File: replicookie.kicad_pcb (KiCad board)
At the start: 4 copper layers, 160 x 120 mm, 161 parts, among them J1001 Conn_01x08_Female, J1002 Screw_Terminal_01x04, J1003 Conn_02x03_Odd_Even, J1004 Conn_01x08_Female, J1101 Conn_01x08_Female, J1102 Screw_Terminal_01x04, J1103 Conn_02x03_Odd_Even, J1104 Conn_01x08_Female, J1201 Conn_01x08_Female, J1202 Screw_Terminal_01x04, J1203 Conn_02x03_Odd_Even, J1204 Conn_01x08_Female, J1301 Conn_01x08_Female, J1302 Screw_Terminal_01x04, J1303 Conn_02x03_Odd_Even, J1304 Conn_01x08_Female, J1401 Conn_01x08_Female, J1402 Screw_Terminal_01x04, J1403 Conn_02x03_Odd_Even, J1404 Conn_01x08_Female, J1501 Conn_01x08_Female, J1502 Screw_Terminal_01x04, J1503 Conn_02x03_Odd_Even, J1504 Conn_01x08_Female, J2 TFM-115-01-F-D-A, J3 TFM-120-01-F-D-A, J301 USB_B_Micro, J401 JK0654219, J501 USB_A, J502 USB_A, J801 Conn_01x08_Female, J802 Screw_Terminal_01x04, J803 Conn_02x03_Odd_Even, J804 Conn_01x08_Female, J901 Conn_01x08_Female, J902 Screw_Terminal_01x04, J903 Conn_02x03_Odd_Even, J904 Conn_01x08_Female, U201 DS1307ZN+, U301 93LCxxBxxOT, U302 FT4232H, U401 MIC33050-4YHL, U402 KSZ9031RNXCA, U403 ASDMB-25.000MHz, U404 74LVC2G07, U501 ASDMB-24.000MHz-C, U502 ASDMB-26.000MHz-C, U503 USB3343, U504 74LVC1G07, U505 USB2514B_Bi, U601 TCA9800, X201 ASE-xxxMHz, Y301 ABM8-12.000MHZ-20

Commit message: Expand PCB, change to inches, center Snickerdoodle
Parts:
- removed R308: 4.7k, Resistor_SMD:R_0603_1608Metric
- removed R309: 10k, Resistor_SMD:R_0603_1608Metric
- added H101: MountingHole, MountingHole:MountingHole_3mm, F.Cu at (130.2, 200.0)
- added H102: MountingHole, MountingHole:MountingHole_3mm, F.Cu at (308.0, 200.0)
- added H103: MountingHole, MountingHole:MountingHole_3mm, F.Cu at (130.2, 79.4)
- added H104: MountingHole, MountingHole:MountingHole_3mm, F.Cu at (308.0, 79.4)
- R301, R302, R303, R304, R305, R306, R307: footprint Resistor_SMD:R_0603_1608Metric -> Resistor_SMD:R_0402_1005Metric
- moved C314 133.5 mm to (144.3, 111.8), turned to -90 degrees
- moved C304 133.5 mm to (142.7, 111.8), turned to -90 degrees
- moved C306 131.6 mm to (133.9, 107.2), turned to 180 degrees
- moved R305 124.6 mm to (136.4, 89.9), turned to 180 degrees
- moved C313 122.2 mm to (144.3, 95.0), turned to 90 degrees
- moved Y301 112.0 mm to (138.2, 113.0), turned to 90 degrees
- moved R306 108.3 mm to (145.3, 111.8), turned to 90 degrees
- moved R307 107.8 mm to (151.4, 101.9)
- moved J301 82.1 mm to (129.7, 91.2), turned to -90 degrees
- moved C401 29.7 mm to (291.0, 132.5)
- moved C402 29.7 mm to (284.2, 132.2)
- moved C403 29.7 mm to (284.2, 135.0)
- moved C404 29.7 mm to (277.7, 135.0)
- moved C405 29.7 mm to (276.0, 135.0)
- moved C406 29.7 mm to (269.2, 123.0)
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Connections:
- net /FTDI/DM renamed /FTDI/D-
- net /FTDI/DP renamed /FTDI/D+
- net Net-(C304-Pad1) renamed /FTDI/VPLL
- net Net-(C305-Pad1) renamed /FTDI/VPHY
- net Net-(R305-Pad1) renamed /FTDI/REF
- net Net-(R306-Pad2) renamed /FTDI/~FTDI_RESET
- U302 pad 26: Net-(U302-Pad26) -> /SWCLK
- U302 pad 27: Net-(U302-Pad27) -> Net-(R307-Pad1)
- U302 pad 28: Net-(U302-Pad28) -> /SWDIO
- U302 pad 29: Net-(U302-Pad29) -> /MCU_~RST
- U302 pad 38: /SWCLK -> /FTDI/FTDI_TX
- U302 pad 39: Net-(R307-Pad1) -> /FTDI/FTDI_RX
- U302 pad 40: /SWDIO -> Net-(U302-Pad40)
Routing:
- net /Ethernet/TXRXB+: track 42.8 -> 0.00 mm
- net /Ethernet/TXRXA-: track 38.9 -> 0.00 mm
- net /Ethernet/TXRXA+: track 38.6 -> 0.00 mm
- net /Ethernet/TXRXB-: track 38.3 -> 0.00 mm
- net /Ethernet/TXRXD+: track 37.0 -> 0.00 mm
- net /Ethernet/TXRXC+: track 35.7 -> 0.00 mm
- net /Ethernet/TXRXD-: track 42.3 -> 7.62 mm
- net /Ethernet/TXRXC-: track 37.2 -> 4.97 mm
- net +3V3: track 30.9 -> 4.85 mm, vias 11 -> 4
- net /Ethernet/LED1: track 21.4 -> 0.00 mm
- net /ETHERNET.MDIO: track 20.1 -> 0.00 mm, vias 1 -> 0
- net /Ethernet/DVDDL: track 23.4 -> 3.31 mm, vias 11 -> 0
- net /ETHERNET.TXD0: track 17.6 -> 0.00 mm
- net /ETHERNET.MDC: track 17.1 -> 0.00 mm, vias 1 -> 0
- net /ETHERNET.TXD1: track 16.1 -> 0.00 mm
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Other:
- board size 160 x 120 mm -> 184.1 x 127 mm

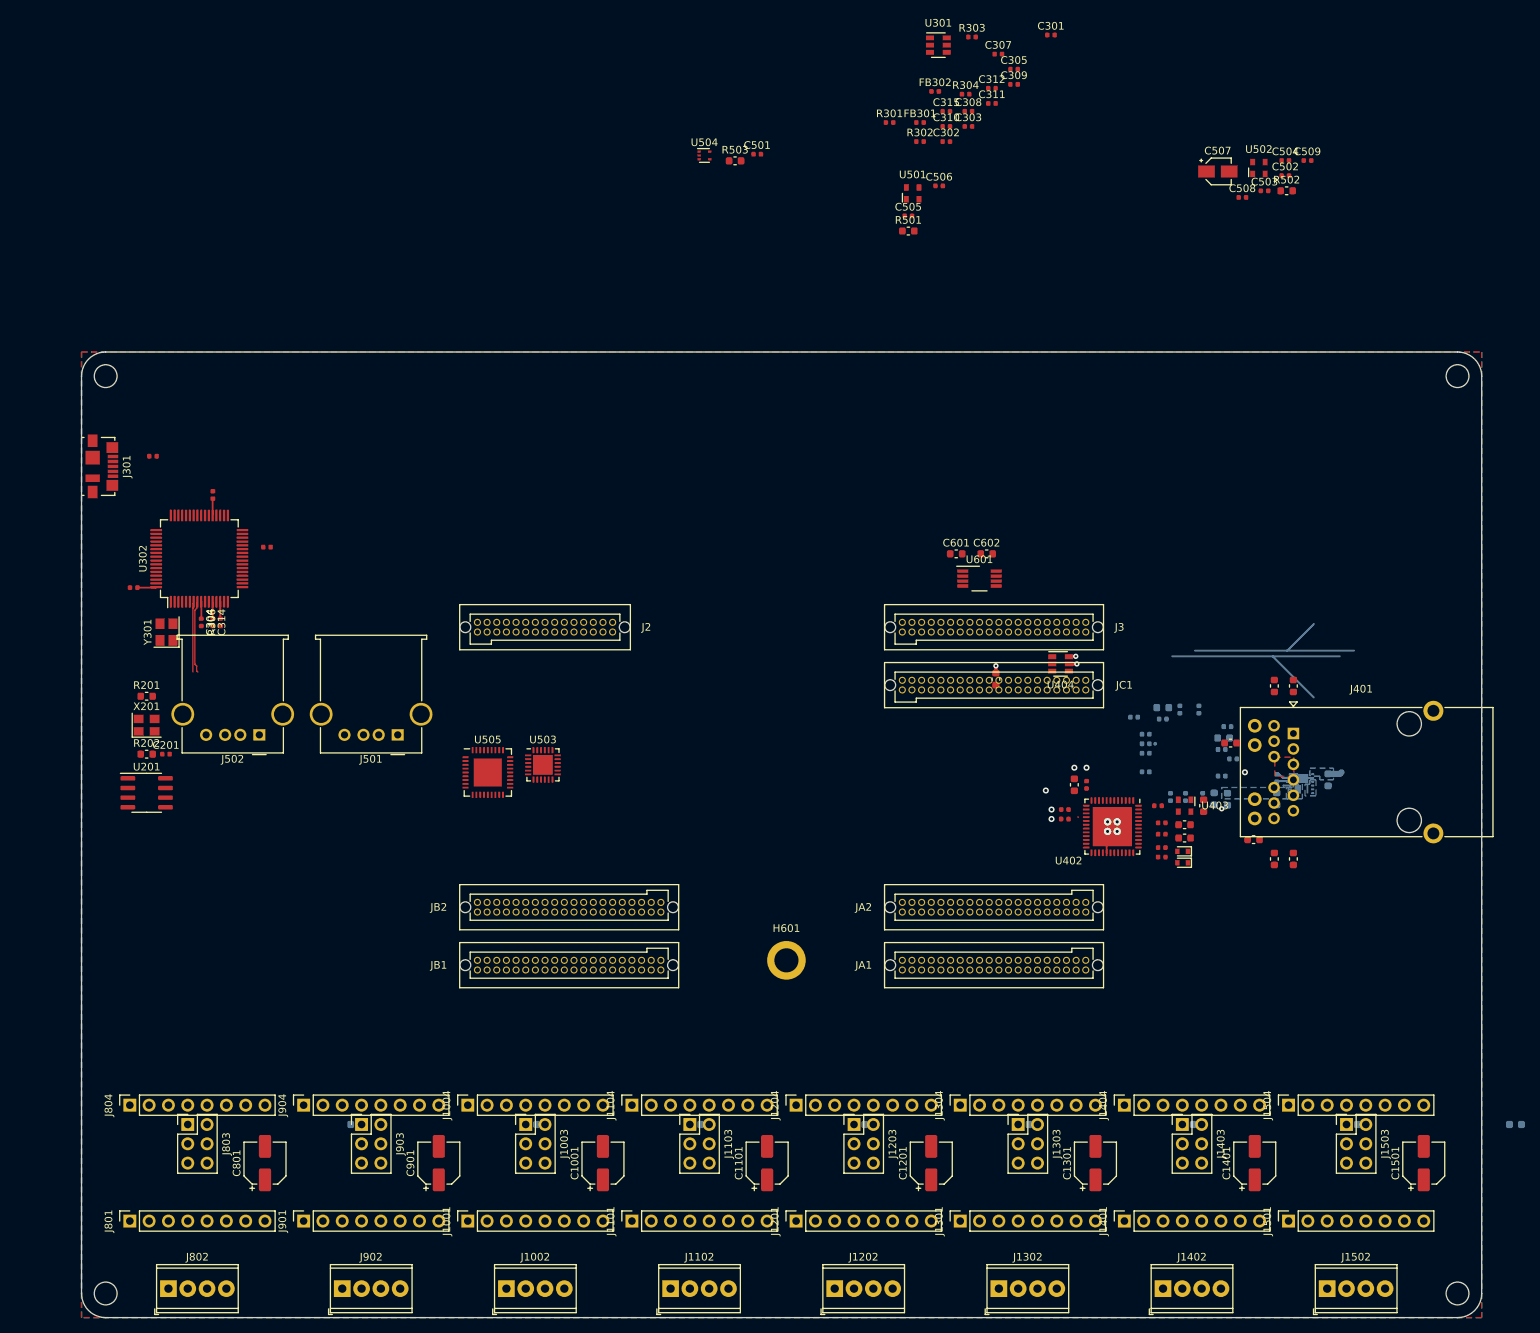
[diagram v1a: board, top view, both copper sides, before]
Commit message: Move Ethernet PHY to left side of board
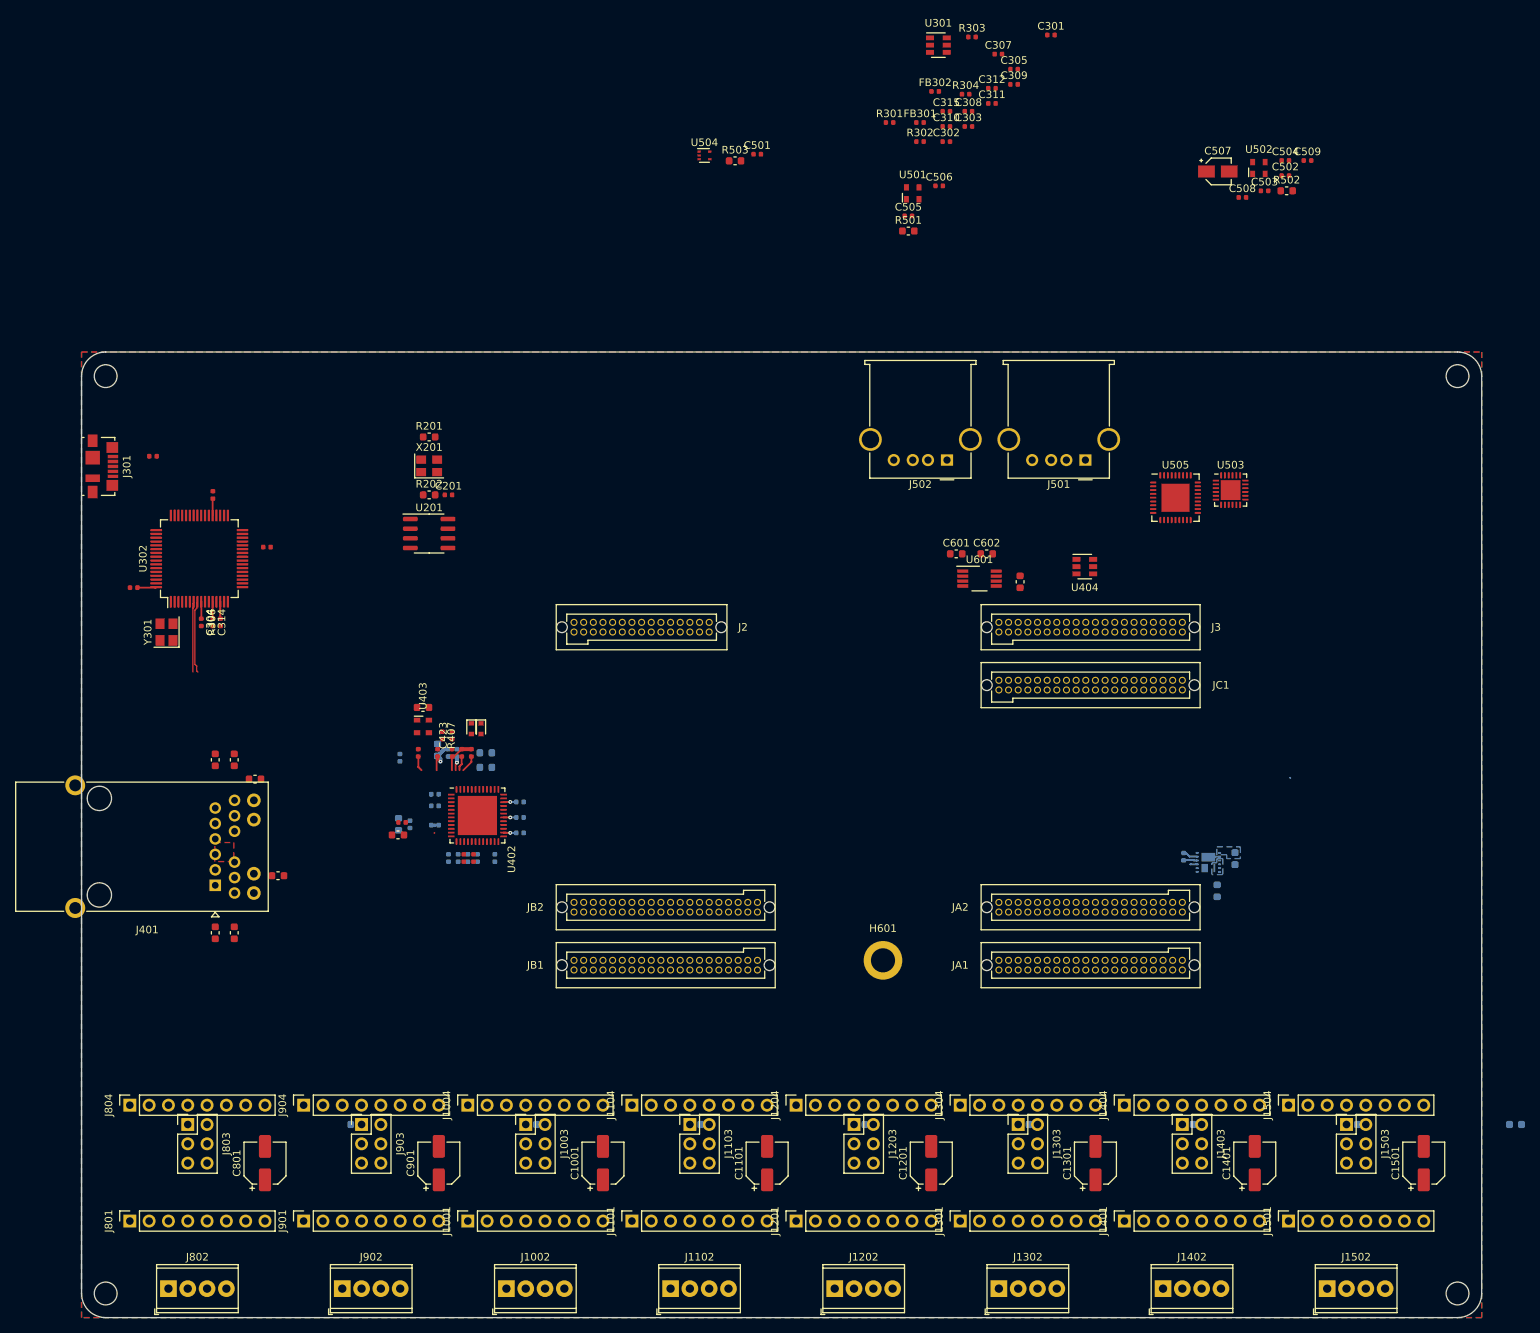
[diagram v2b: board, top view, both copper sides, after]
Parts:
- C423: footprint Capacitor_SMD:C_0603_1608Metric -> Capacitor_SMD:C_0402_1005Metric
- R407: footprint Resistor_SMD:R_0603_1608Metric -> Resistor_SMD:R_0402_1005Metric
- moved C426 145.5 mm to (144.6, 152.6), turned to -90 degrees
- moved J401 143.2 mm to (144.6, 146.3), turned to 180 degrees
- moved C427 142.4 mm to (144.6, 129.8), turned to 90 degrees
- moved C425 140.6 mm to (147.1, 152.6), turned to -90 degrees
- moved C428 137.4 mm to (147.1, 129.8), turned to 90 degrees
- moved R409 131.6 mm to (149.8, 132.4), turned to 0 degrees
- moved R408 126.5 mm to (152.8, 145.1), turned to 0 degrees
- moved R401 109.6 mm to (168.9, 129.6), turned to -90 degrees
- moved C411 104.6 mm to (173.5, 134.4), turned to 180 degrees
- moved C422 103.5 mm to (171.9, 122.9), turned to 180 degrees
- moved C407 103.4 mm to (173.8, 128.5), turned to 90 degrees
- moved FB402 101.7 mm to (175.2, 128.9), turned to -90 degrees
- moved C406 101.7 mm to (168.7, 138.3), turned to -90 degrees
- moved C414 101.3 mm to (173.5, 135.9), turned to 180 degrees
- moved U403 100.7 mm to (171.9, 125.4), turned to -90 degrees
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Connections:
- JA2 pad 12: /ETHERNET.TXD3 -> Net-(JA2-Pad12)
- JA2 pad 14: /ETHERNET.TX_CLK -> Net-(JA2-Pad14)
- JA2 pad 18: /ETHERNET.TX_CTL -> Net-(JA2-Pad18)
- JA2 pad 20: /ETHERNET.RXD3 -> Net-(JA2-Pad20)
- JA2 pad 24: /ETHERNET.RXD2 -> Net-(JA2-Pad24)
- JA2 pad 26: /ETHERNET.RXD1 -> Net-(JA2-Pad26)
- JA2 pad 30: /ETHERNET.RXD0 -> Net-(JA2-Pad30)
- JA2 pad 32: /ETHERNET.RX_CTL -> Net-(JA2-Pad32)
- JA2 pad 35: /ETHERNET.MDIO -> Net-(JA2-Pad35)
- JA2 pad 36: /ETHERNET.RX_CLK -> Net-(JA2-Pad36)
- JA2 pad 37: /ETHERNET.MDC -> Net-(JA2-Pad37)
- JA2 pad 38: /~ETHERNET_RST -> Net-(JA2-Pad38)
- JA2 pad 4: /ETHERNET.TXD0 -> Net-(JA2-Pad4)
- JA2 pad 6: /ETHERNET.TXD1 -> Net-(JA2-Pad6)
- JA2 pad 8: /ETHERNET.TXD2 -> Net-(JA2-Pad8)
- JB2 pad 12: Net-(JB2-Pad12) -> /ETHERNET.TXD3
- JB2 pad 14: Net-(JB2-Pad14) -> /ETHERNET.TX_CLK
- JB2 pad 18: Net-(JB2-Pad18) -> /ETHERNET.TX_CTL
- JB2 pad 20: Net-(JB2-Pad20) -> /ETHERNET.RXD3
- JB2 pad 24: Net-(JB2-Pad24) -> /ETHERNET.RXD2
- JB2 pad 26: Net-(JB2-Pad26) -> /ETHERNET.RXD1
- JB2 pad 30: Net-(JB2-Pad30) -> /ETHERNET.RXD0
- JB2 pad 32: Net-(JB2-Pad32) -> /ETHERNET.RX_CTL
- JB2 pad 35: Net-(JB2-Pad35) -> /ETHERNET.MDIO
- JB2 pad 36: Net-(JB2-Pad36) -> /ETHERNET.RX_CLK
- JB2 pad 37: Net-(JB2-Pad37) -> /ETHERNET.MDC
- JB2 pad 38: Net-(JB2-Pad38) -> /~ETHERNET_RST
- JB2 pad 4: Net-(JB2-Pad4) -> /ETHERNET.TXD0
- JB2 pad 6: Net-(JB2-Pad6) -> /ETHERNET.TXD1
- JB2 pad 8: Net-(JB2-Pad8) -> /ETHERNET.TXD2
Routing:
- net GND: track 25.3 -> 1.41 mm, vias 9 -> 0
- net /Ethernet/LED1K: track 23.2 -> 0.00 mm, vias 1 -> 0
- net /Ethernet/LED2K: track 20.9 -> 0.00 mm
- net /Ethernet/TXRXD-: track 7.62 -> 0.00 mm
- net /Ethernet/AVDDL_PLL: track 0.00 -> 5.32 mm, vias 0 -> 1
- net /Ethernet/TXRXC-: track 4.97 -> 0.00 mm
- net /Ethernet/DVDDL: track 3.31 -> 8.09 mm, vias 0 -> 3
- net +3V3: track 4.85 -> 7.31 mm, vias 4 -> 1
- net /ETHERNET.MDIO: track 0.00 -> 2.23 mm
- net /Ethernet/ISET: track 0.00 -> 1.97 mm
- net /Ethernet/~INT~/~PME2: track 0.00 -> 1.91 mm
- removed copper zone on B.Cu, net /Ethernet/DVDDL
- removed copper zone on In2.Cu, net /Ethernet/DVDDL
